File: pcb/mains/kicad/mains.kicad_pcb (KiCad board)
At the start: 2 copper layers, 150 x 110 mm, 26 parts, among them J1 1868076, J2 1868076, J3 1868076, J4 1868076, J5 43650-0300, J6 43045-0200, K1 G5RL-1A-TV8 DC5, U1 IRM-45-12, U2 AP63205WU-7

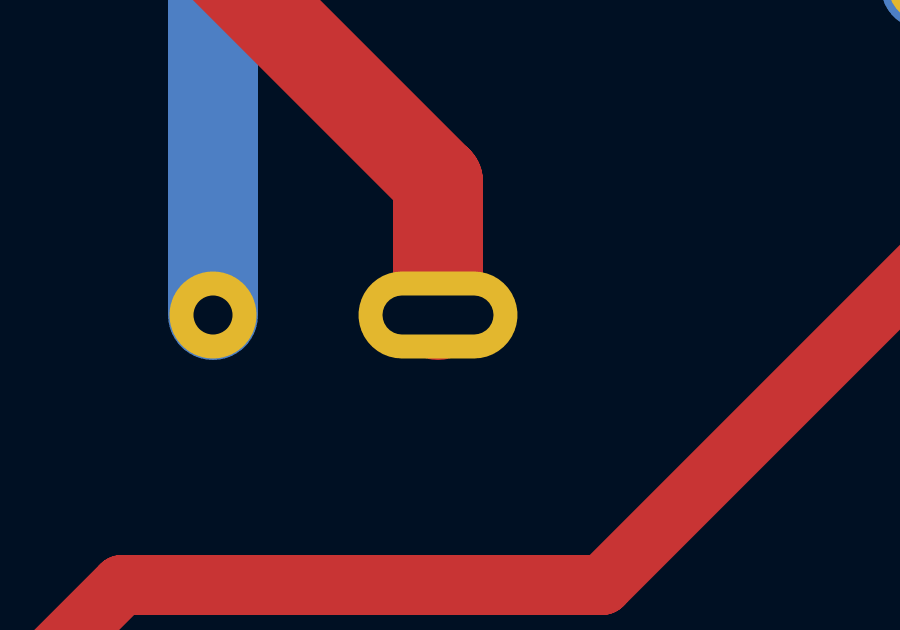
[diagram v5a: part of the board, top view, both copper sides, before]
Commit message: Fit the bulk MOV and refresh mains fabrication outputs
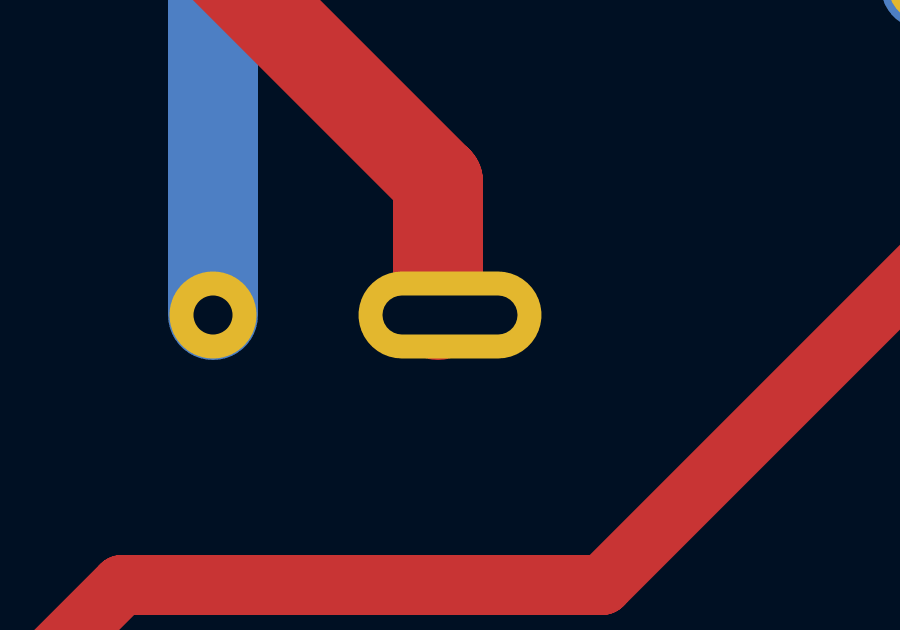
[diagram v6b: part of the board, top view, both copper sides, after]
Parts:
- RV1: value TMOV14RP175EL2T7 -> TMOV14RP175E
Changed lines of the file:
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@@
 			)
 		)
-		(property "Value" "TMOV14RP175EL2T7"
+		(property "Value" "TMOV14RP175E"
 			(at 0 3 0)
 			(layer "F.Fab")
@@
 			)
 		)
-		(property "MPN" "TMOV14RP175EL2T7"
+		(property "MPN" "TMOV14RP175E"
 			(at 0 0 0)
 			(layer "F.SilkS")
@@
 		)
 		(pad "2" thru_hole oval
-			(at 7.5 0)
-			(size 5.3 2.9)
-			(drill oval 3.7 1.3)
+			(at 7.9 0)
+			(size 6.1 2.9)
+			(drill oval 4.5 1.3)
 			(layers "*.Cu" "*.Mask")
 			(remove_unused_layers no)
@@
 		(polygon
 			(pts
-				(xy 64.099999 117.55) (xy 71.4 117.55) (xy 71.4 122.45) (xy 64.099999 122.45)
+				(xy 64.099999 117.55) (xy 72.2 117.55) (xy 72.2 122.45) (xy 64.099999 122.45)
 			)
 		)
